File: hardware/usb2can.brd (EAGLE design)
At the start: 39.1 x 34.8 mm, 43 parts, among them IC1 7805TV, U1 ATMEGA32U4, U2 MCP2551SN, U3 MCP2510SO, X2 USB-A-S

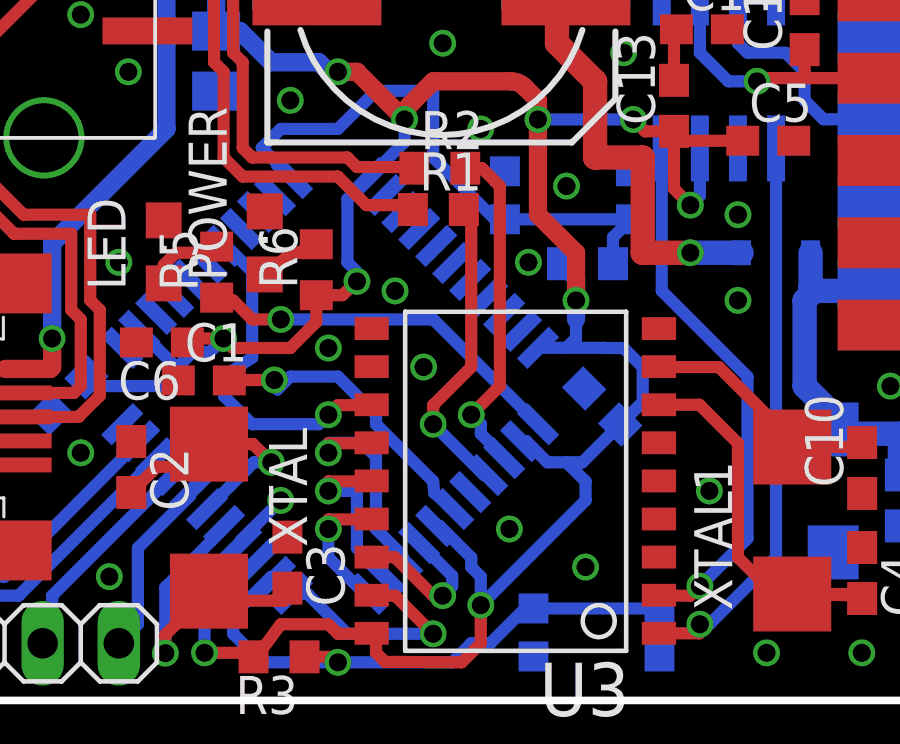
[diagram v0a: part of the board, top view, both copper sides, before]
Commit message: added the CAN Start of Frame signal path to pcb
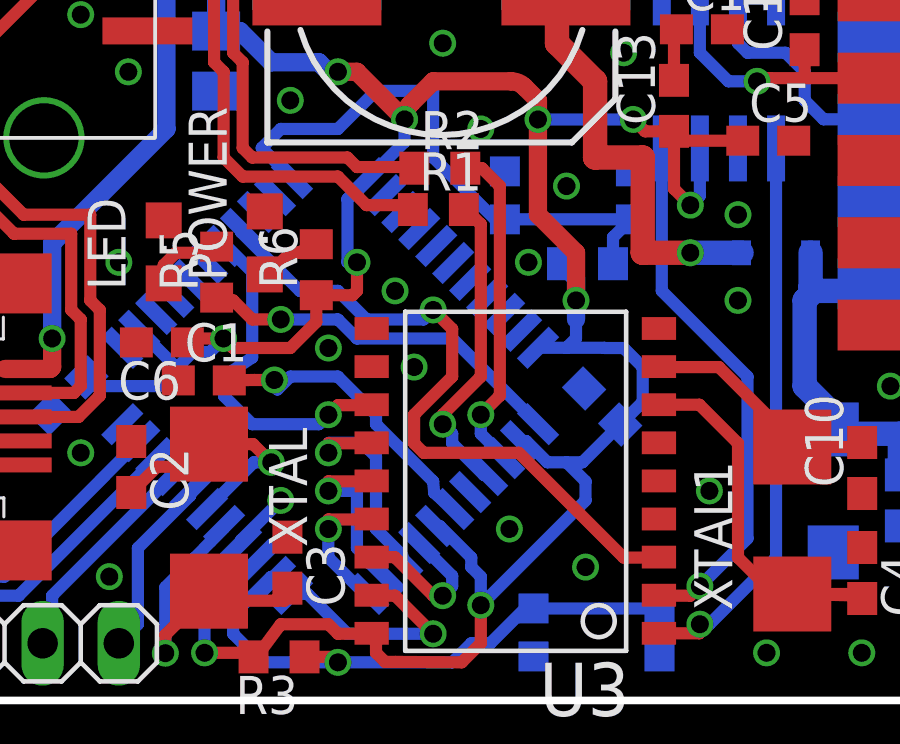
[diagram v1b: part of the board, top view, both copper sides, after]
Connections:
- new net CAN_SOF: U1.30, U3.3
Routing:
- net CAN_SOF: track 0.00 -> 22.8 mm, vias 0 -> 1
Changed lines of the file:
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@@
 <wire x1="20.0025" y1="28.8925" x2="20.0025" y2="30.48" width="0.6096" layer="1"/>
 <wire x1="20.0025" y1="30.48" x2="19.685" y2="30.7975" width="0.6096" layer="1"/>
-<wire x1="18.3295" y1="13.507" x2="19.1955" y2="13.507" width="0.4064" layer="1"/>
-<wire x1="19.1955" y1="13.507" x2="19.685" y2="13.97" width="0.4064" layer="1"/>
-<via x="19.685" y="13.97" extent="1-16" drill="0.6" shape="square"/>
-<wire x1="19.685" y1="13.97" x2="19.685" y2="14.2875" width="0.4064" layer="16"/>
-<wire x1="19.685" y1="14.2875" x2="19.3675" y2="14.605" width="0.4064" layer="16"/>
+<wire x1="18.3295" y1="13.507" x2="19.5395" y2="13.507" width="0.4064" layer="1"/>
+<wire x1="19.5395" y1="13.507" x2="19.685" y2="13.6525" width="0.4064" layer="1"/>
+<wire x1="19.685" y1="13.6525" x2="19.685" y2="14.605" width="0.4064" layer="1"/>
+<via x="19.685" y="14.605" extent="1-16" drill="0.6" shape="square"/>
+<wire x1="19.685" y1="14.605" x2="19.3675" y2="14.605" width="0.4064" layer="16"/>
 <wire x1="19.3675" y1="14.605" x2="19.3675" y2="16.71435" width="0.4064" layer="16"/>
 <wire x1="19.3675" y1="16.71435" x2="20.06479375" y2="17.41164375" width="0.4064" layer="16"/>
@@
 <contactref element="C12" pad="-"/>
 <contactref element="C14" pad="2"/>
-<via x="21.9075" y="11.1125" extent="1-16" drill="0.6" shape="square"/>
 <via x="32.385" y="16.1925" extent="1-16" drill="0.6" shape="square"/>
 <via x="32.385" y="13.335" extent="1-16" drill="0.6" shape="square"/>
@@
 <via x="26.67" y="17.145" extent="1-16" drill="0.6" shape="square"/>
 <via x="25.4" y="14.605" extent="1-16" drill="0.6" shape="square"/>
+<via x="21.59" y="11.1125" extent="1-16" drill="0.6" shape="octagon"/>
 </signal>
 <signal name="N$7">
@@
 <contactref element="R1" pad="2"/>
 <wire x1="23.248" y1="16.363" x2="23.3245" y2="16.363" width="0.4064" layer="1"/>
-<wire x1="23.3245" y1="16.363" x2="23.495" y2="15.875" width="0.4064" layer="1"/>
-<wire x1="23.495" y1="15.875" x2="23.495" y2="11.1125" width="0.4064" layer="1"/>
-<wire x1="23.495" y1="11.1125" x2="22.225" y2="9.8425" width="0.4064" layer="1"/>
-<wire x1="22.225" y1="9.8425" x2="22.225" y2="9.2075" width="0.4064" layer="1"/>
-<via x="22.225" y="9.2075" extent="1-16" drill="0.6" shape="square"/>
+<wire x1="23.3245" y1="16.363" x2="23.8125" y2="15.875" width="0.4064" layer="1"/>
+<wire x1="23.8125" y1="15.875" x2="23.8125" y2="10.795" width="0.4064" layer="1"/>
+<wire x1="23.8125" y1="10.795" x2="22.5425" y2="9.525" width="0.4064" layer="1"/>
+<wire x1="22.5425" y1="9.525" x2="22.5425" y2="9.2075" width="0.4064" layer="1"/>
+<via x="22.5425" y="9.2075" extent="1-16" drill="0.6" shape="octagon"/>
 <wire x1="24.024590625" y1="7.51215" x2="23.92035" y2="7.51215" width="0.4064" layer="16"/>
-<wire x1="23.92035" y1="7.51215" x2="22.225" y2="9.2075" width="0.4064" layer="16"/>
+<wire x1="23.92035" y1="7.51215" x2="22.86" y2="8.5725" width="0.4064" layer="16"/>
+<wire x1="22.86" y1="8.5725" x2="22.86" y2="8.89" width="0.4064" layer="16"/>
+<wire x1="22.86" y1="8.89" x2="22.5425" y2="9.2075" width="0.4064" layer="16"/>
 </signal>
 <signal name="N$10">
 <contactref element="U1" pad="3"/>
 <contactref element="R2" pad="2"/>
-<wire x1="24.4475" y1="17.145" x2="24.4475" y2="10.4775" width="0.4064" layer="1"/>
-<wire x1="24.4475" y1="10.4775" x2="23.495" y2="9.525" width="0.4064" layer="1"/>
-<via x="23.495" y="9.525" extent="1-16" drill="0.6" shape="square"/>
+<wire x1="24.4475" y1="17.145" x2="24.4475" y2="10.16" width="0.4064" layer="1"/>
+<wire x1="24.4475" y1="10.16" x2="23.8125" y2="9.525" width="0.4064" layer="1"/>
+<via x="23.8125" y="9.525" extent="1-16" drill="0.6" shape="octagon"/>
 <wire x1="23.2955" y1="17.7405" x2="23.852" y2="17.7405" width="0.4064" layer="1"/>
 <wire x1="23.852" y1="17.7405" x2="24.4475" y2="17.145" width="0.4064" layer="1"/>
 <wire x1="24.590278125" y1="8.077834375" x2="24.590278125" y2="8.112221875" width="0.4064" layer="16"/>
 <wire x1="24.590278125" y1="8.112221875" x2="23.8125" y2="8.89" width="0.4064" layer="16"/>
-<wire x1="23.8125" y1="8.89" x2="23.8125" y2="9.2075" width="0.4064" layer="16"/>
-<wire x1="23.8125" y1="9.2075" x2="23.495" y2="9.525" width="0.4064" layer="16"/>
+<wire x1="23.8125" y1="8.89" x2="23.8125" y2="9.525" width="0.4064" layer="16"/>
 </signal>
 <signal name="D+">
@@
 <wire x1="16.1925" y1="12.7" x2="17.145" y2="12.7" width="0.4064" layer="1"/>
 <via x="17.145" y="12.7" extent="1-16" drill="0.6" shape="octagon"/>
-<wire x1="17.145" y1="12.7" x2="22.230853125" y2="12.7" width="0.4064" layer="16"/>
-<wire x1="22.230853125" y1="12.7" x2="25.721646875" y2="9.20920625" width="0.4064" layer="16"/>
+<wire x1="17.145" y1="12.7" x2="19.05" y2="12.7" width="0.4064" layer="16"/>
+<wire x1="19.05" y1="12.7" x2="19.685" y2="12.065" width="0.4064" layer="16"/>
+<wire x1="19.685" y1="12.065" x2="22.865853125" y2="12.065" width="0.4064" layer="16"/>
+<wire x1="22.865853125" y1="12.065" x2="25.721646875" y2="9.20920625" width="0.4064" layer="16"/>
 <wire x1="15.5575" y1="13.335" x2="15.101" y2="13.335" width="0.4064" layer="1"/>
 <wire x1="15.101" y1="13.335" x2="15.008" y2="13.428" width="0.4064" layer="1"/>
@@
 <via x="4.1275" y="15.875" extent="1-16" drill="0.6" shape="square"/>
 </signal>
+<signal name="CAN_SOF">
+<contactref element="U3" pad="3"/>
+<contactref element="U1" pad="30"/>
+<wire x1="15.822153125" y1="15.7145875" x2="15.822153125" y2="15.610346875" width="0.4064" layer="16"/>
+<wire x1="15.822153125" y1="15.610346875" x2="17.78" y2="13.6525" width="0.4064" layer="16"/>
+<wire x1="17.78" y1="13.6525" x2="19.05" y2="13.6525" width="0.4064" layer="16"/>
+<wire x1="19.05" y1="13.6525" x2="20.0025" y2="12.7" width="0.4064" layer="16"/>
+<wire x1="20.0025" y1="12.7" x2="21.9075" y2="12.7" width="0.4064" layer="16"/>
+<wire x1="21.9075" y1="12.7" x2="22.225" y2="13.0175" width="0.4064" layer="16"/>
+<via x="22.225" y="13.0175" extent="1-16" drill="0.6" shape="octagon"/>
+<wire x1="22.225" y1="13.0175" x2="22.86" y2="12.3825" width="0.4064" layer="1"/>
+<wire x1="22.86" y1="12.3825" x2="22.86" y2="10.795" width="0.4064" layer="1"/>
+<wire x1="22.86" y1="10.795" x2="21.59" y2="9.525" width="0.4064" layer="1"/>
+<wire x1="21.59" y1="9.525" x2="21.59" y2="8.5725" width="0.4064" layer="1"/>
+<wire x1="21.59" y1="8.5725" x2="21.9075" y2="8.255" width="0.4064" layer="1"/>
+<wire x1="21.9075" y1="8.255" x2="25.0825" y2="8.255" width="0.4064" layer="1"/>
+<wire x1="25.0825" y1="8.255" x2="28.575" y2="4.7625" width="0.4064" layer="1"/>
+<wire x1="28.575" y1="4.7625" x2="29.7354" y2="4.7625" width="0.4064" layer="1"/>
+<wire x1="29.7354" y1="4.7625" x2="29.7504" y2="4.7775" width="0.4064" layer="1"/>
+</signal>
 </signals>
